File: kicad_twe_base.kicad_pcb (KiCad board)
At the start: 2 copper layers, 72 x 47.5 mm, 18 parts, among them U1 TWE-L-DP-W

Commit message: シルク修正
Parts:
- turned ~ to 180 degrees
- renumbered SW3 to BATT←→CONN, SW2 to RST, SW1 to locked, J2 to ~, J1 to ~, JP1 to ~
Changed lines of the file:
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@@
     (property "Sheetname" "")
     (attr through_hole)
-    (fp_text reference "J2" (at 0 -2.33) (layer "F.SilkS")
+    (fp_text reference "~" (at 0 -2.33) (layer "F.SilkS")
       (effects (font (size 1 1) (thickness 0.15)))
     )
@@
     (property "Sheetname" "")
     (attr through_hole)
-    (fp_text reference "J1" (at 0 -2.33) (layer "F.SilkS")
+    (fp_text reference "~" (at 0 -2.33) (layer "F.SilkS")
       (effects (font (size 1 1) (thickness 0.15)))
     )
@@
     (property "Sheetname" "")
     (attr through_hole)
-    (fp_text reference "SW3" (at 4.9875 -5.08) (layer "F.SilkS")
-      (effects (font (size 1 1) (thickness 0.15)))
+    (fp_text reference "BATT←→CONN" (at 4.9875 -5.08) (layer "F.SilkS")
+      (effects (font (size 1 1) (thickness 0.1)))
     )
     (fp_text value "~" (at 5.08 1.27) (layer "F.Fab")
@@
     (property "Sheetname" "")
     (attr through_hole)
-    (fp_text reference "SW1" (at 5.0075 -4.8475 -90 unlocked) (layer "F.SilkS")
-      (effects (font (size 1 1) (thickness 0.15)))
+    (fp_text reference locked "RUN←→PRG" (at 5.0075 -4.8475 -90 unlocked) (layer "F.SilkS")
+      (effects (font (size 1 1) (thickness 0.1)))
     )
     (fp_text value "~" (at 5.08 1.27 90) (layer "F.Fab")
@@
     (property "Sheetname" "")
     (attr through_hole)
-    (fp_text reference "SW2" (at 7.62 2.54 180) (layer "F.SilkS")
-      (effects (font (size 1 1) (thickness 0.15)))
+    (fp_text reference "RST" (at 7.62 2.54 180) (layer "F.SilkS")
+      (effects (font (size 1 1) (thickness 0.1)))
     )
     (fp_text value "~" (at 5.08 -5.08) (layer "F.Fab")
@@
   )
   (footprint "Jumper:SolderJumper-3_P1.3mm_Open_RoundedPad1.0x1.5mm_NumberLabels" (layer "F.Cu")
-    (at 33.02 -41.2925)
+    (at 33.02 -41.2925 180)
     (descr "SMD Solder 3-pad Jumper, 1x1.5mm rounded Pads, 0.3mm gap, open, labeled with numbers")
     (tags "solder jumper open")
@@
     (property "Sheetname" "")
     (attr exclude_from_pos_files)
-    (fp_text reference "JP1" (at 0 -1.8) (layer "F.SilkS")
+    (fp_text reference "~" (at 0 -1.8) (layer "F.SilkS")
       (effects (font (size 1 1) (thickness 0.15)))
     )
@@
     (fp_line (start 2.3 1.25) (end 2.3 -1.25) (layer "F.CrtYd") (width 0.05))
     (fp_line (start -2.3 -1.25) (end -2.3 1.25) (layer "F.CrtYd") (width 0.05))
-    (pad "1" smd custom locked (at -1.3 0) (size 1 0.5) (layers "F.Cu" "F.Mask")
+    (pad "1" smd custom locked (at -1.3 0 180) (size 1 0.5) (layers "F.Cu" "F.Mask")
       (net 28 "Net-(J3-Pad6)") (pinfunction "A") (pintype "passive") (zone_connect 2)
       (options (clearance outline) (anchor rect))
@@
           ) (width 0) (fill yes))
       ))
-    (pad "2" smd rect locked (at 0 0) (size 1 1.5) (layers "F.Cu" "F.Mask")
+    (pad "2" smd rect locked (at 0 0 180) (size 1 1.5) (layers "F.Cu" "F.Mask")
       (net 14 "+3V3") (pinfunction "C") (pintype "input"))
-    (pad "3" smd custom locked (at 1.3 0) (size 1 0.5) (layers "F.Cu" "F.Mask")
+    (pad "3" smd custom locked (at 1.3 0 180) (size 1 0.5) (layers "F.Cu" "F.Mask")
       (net 29 "Net-(JP1-Pad3)") (pinfunction "B") (pintype "passive") (zone_connect 2)
       (options (clearance outline) (anchor rect))

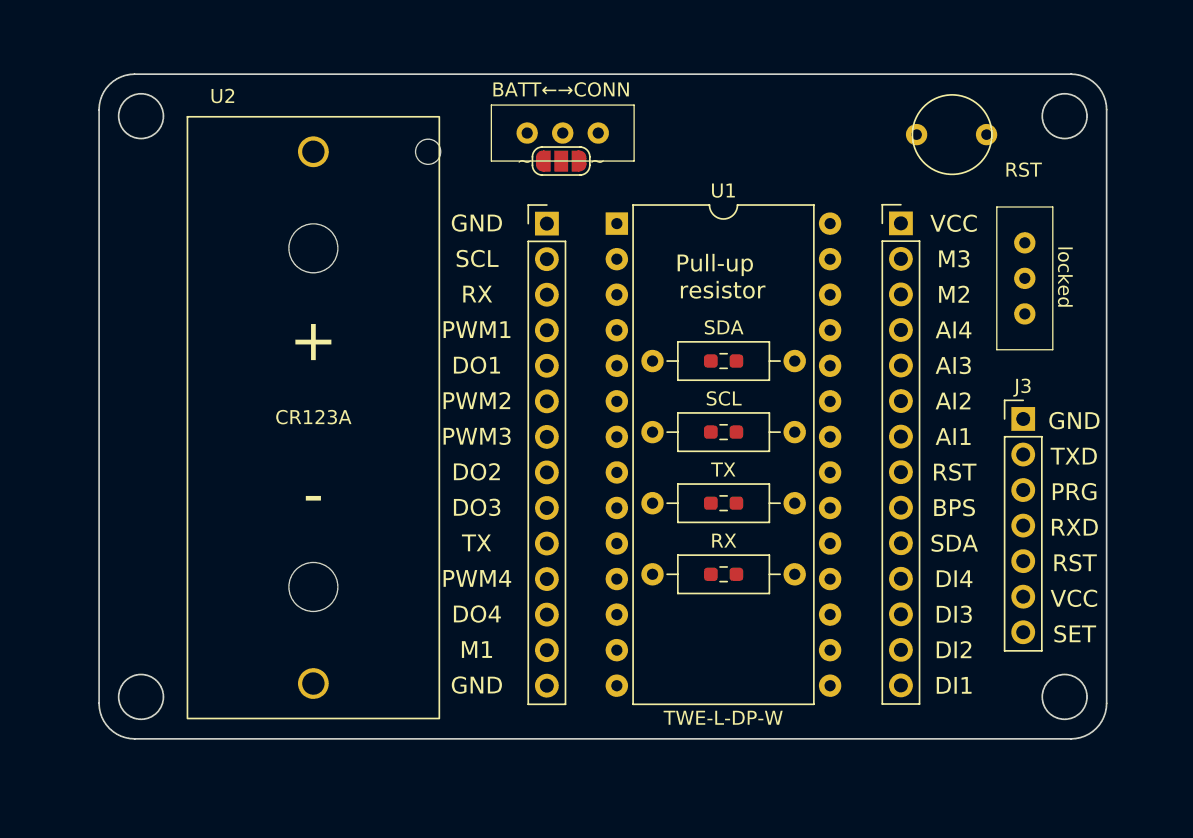
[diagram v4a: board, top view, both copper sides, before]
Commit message: 配線完了 DRC OK
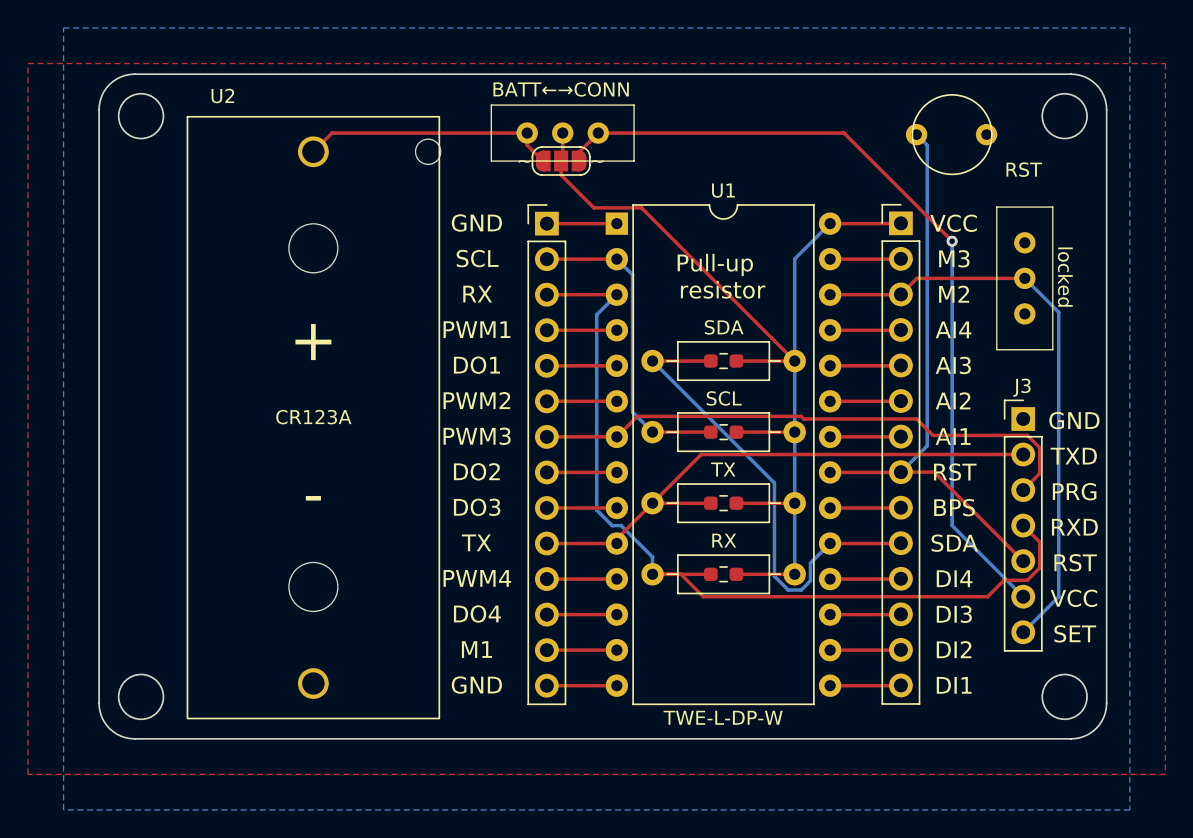
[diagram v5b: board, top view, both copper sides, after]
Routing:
- net +3V3: track 0.00 -> 73.1 mm
- net Net-(J1-Pad3): track 0.00 -> 64.5 mm
- net Net-(J3-Pad6): track 0.00 -> 58.6 mm, vias 0 -> 1
- net Net-(J2-Pad3): track 0.00 -> 41.7 mm
- net Net-(J2-Pad8): track 0.00 -> 41.7 mm
- net Net-(J1-Pad10): track 0.00 -> 41.0 mm
- net Net-(J1-Pad7): track 0.00 -> 40.3 mm
- net Net-(J2-Pad10): track 0.00 -> 34.7 mm
- net Net-(J1-Pad2): track 0.00 -> 22.6 mm
- net Net-(JP1-Pad3): track 0.00 -> 18.3 mm
- net GND: track 0.00 -> 10.0 mm
- net Net-(J2-Pad7): track 0.00 -> 5.07 mm
- net Net-(J2-Pad14): track 0.00 -> 5.07 mm
- net Net-(J2-Pad13): track 0.00 -> 5.07 mm
- net Net-(J2-Pad9): track 0.00 -> 5.07 mm
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- added copper zone on B.Cu, net GND
- added copper zone on F.Cu, net GND
